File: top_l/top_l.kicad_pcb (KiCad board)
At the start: 2 copper layers, 128.4 x 119.3 mm, 31 parts, among them SW29 SW_Push, SW30 SW_Push, SW31 SW_Push, SW32 SW_Push, SW33 SW_Push, SW34 SW_Push, SW35 SW_Push, SW36 SW_Push, SW37 SW_Push, SW38 SW_Push, SW39 SW_Push, SW40 SW_Push, SW41 SW_Push, SW42 SW_Push, SW43 SW_Push, SW44 SW_Push, SW45 SW_Push, SW46 SW_Push, SW47 SW_Push, SW48 SW_Push, SW49 SW_Push, SW50 SW_Push, SW51 SW_Push, SW52 SW_Push, SW53 SW_Push, SW54 SW_Push, SW55 SW_Push

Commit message: feat: add switch plate
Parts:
- moved SW52 115.8 mm to (86.0, 66.9)
- moved SW53 115.8 mm to (86.0, 83.4)
- moved SW54 115.8 mm to (86.0, 99.9)
- moved SW55 115.8 mm to (86.0, 116.4)
- moved Ref** 99.2 mm to (94.3, 46.3)
- moved Ref** 90.9 mm to (189.3, 124.3)
- moved SW48 82.8 mm to (102.5, 66.9)
- moved SW49 82.8 mm to (102.5, 83.4)
- moved SW50 82.8 mm to (102.5, 99.9)
- moved SW51 82.8 mm to (102.5, 116.4)
- moved SW33 62.9 mm to (175.3, 136.8), turned to -15 degrees
- moved Ref** 58.9 mm to (173.3, 42.3)
- moved Ref** 54.2 mm to (116.8, 122.8)
- moved SW44 49.7 mm to (119.1, 50.5)
- moved SW45 49.7 mm to (119.1, 67.0)
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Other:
- outline, holes or cut-outs redrawn

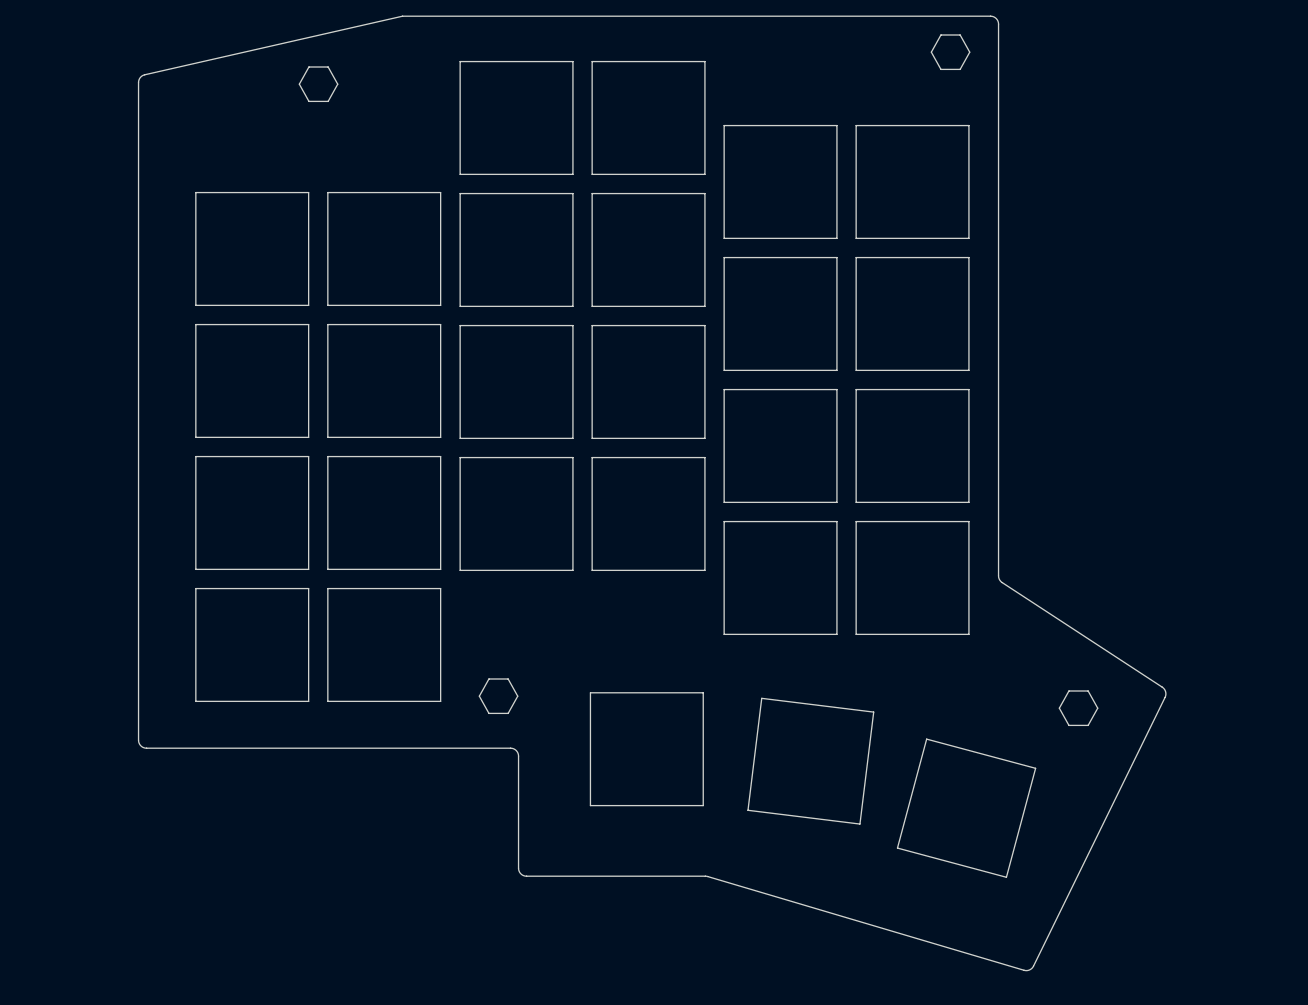
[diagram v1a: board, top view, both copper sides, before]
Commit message: feat: add hole to switch plate
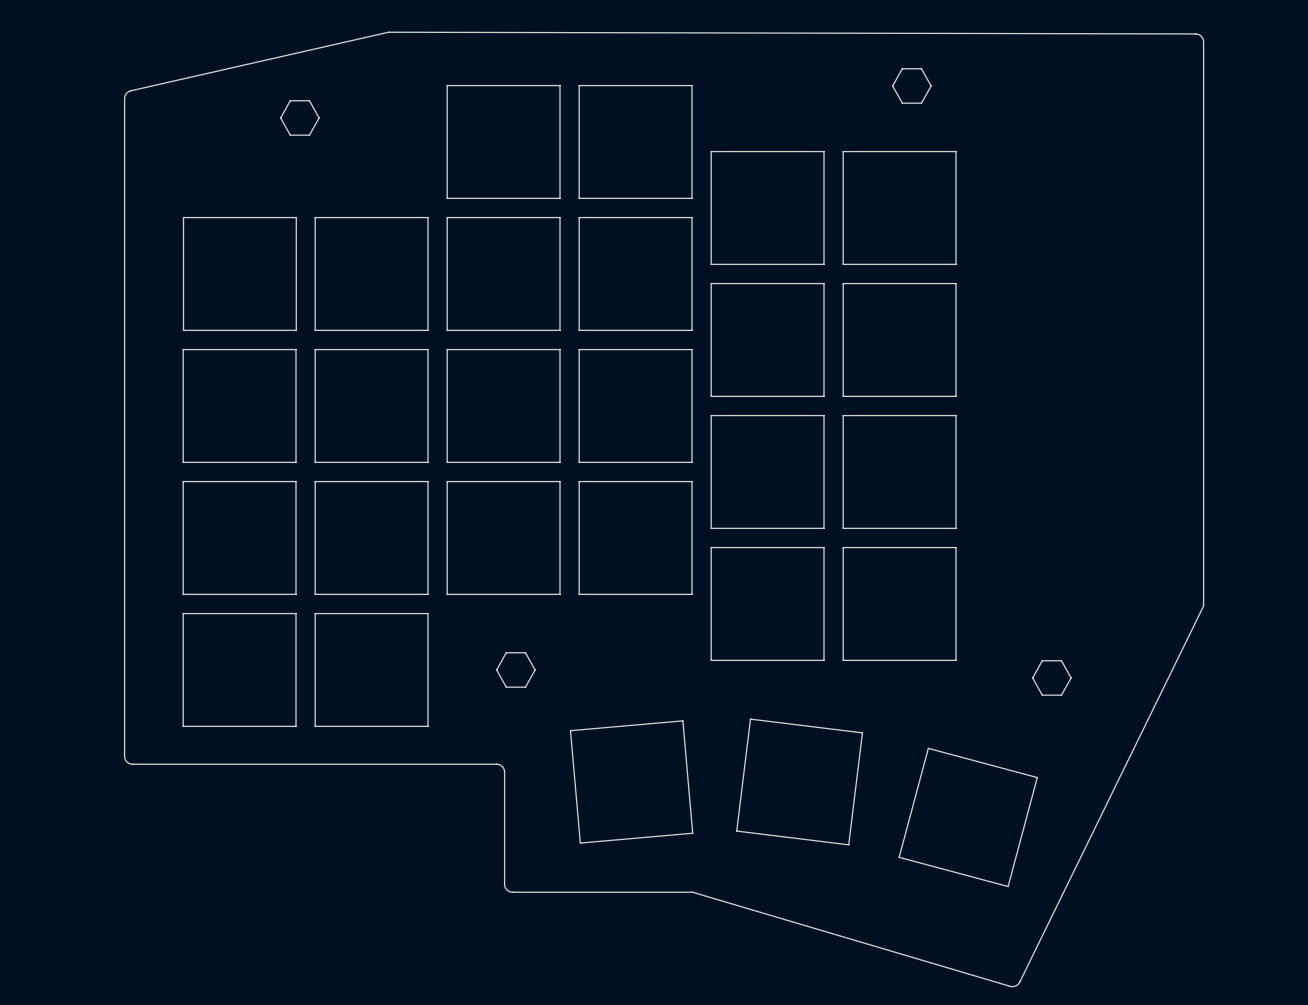
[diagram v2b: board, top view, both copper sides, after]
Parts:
- removed the Ref** at (173.3, 42.3)
- removed the Ref** at (189.3, 124.3)
- removed the Ref** at (94.3, 46.3)
- removed the Ref** at (116.8, 122.8)
- removed SW29, SW30, SW31, SW32, SW33, SW34, SW35, SW36, SW37, SW38, SW39, SW40, SW41, SW42, SW43, SW44, SW45, SW46, SW47, SW48, SW49, SW50, SW51, SW52, SW53, SW54, SW55: SW_Push, kbd_SW_Hole:SW_Hole_1u_16.5
- added Ref**: Val**, kbd_Hole:m2_Spacer_Hole_hex, F.Cu at (186.0, 120.5)
- added Ref**: Val**, kbd_Hole:m2_Spacer_Hole_hex, F.Cu at (92.0, 50.5)
- added Ref**: Val**, kbd_Hole:m2_Spacer_Hole_hex, F.Cu at (119.0, 119.5)
- added Ref**: Val**, kbd_Hole:m2_Spacer_Hole_hex, F.Cu at (168.5, 46.5)
- added SW1: SW_Push, kbd_SW_Hole:SW_Hole_1u_16.5, F.Cu at (84.5, 70.0)
- added SW10: SW_Push, kbd_SW_Hole:SW_Hole_1u_16.5, F.Cu at (134.0, 70.0)
- added SW11: SW_Push, kbd_SW_Hole:SW_Hole_1u_16.5, F.Cu at (150.5, 78.2)
- added SW12: SW_Push, kbd_SW_Hole:SW_Hole_1u_16.5, F.Cu at (167.0, 78.2)
- added SW13: SW_Push, kbd_SW_Hole:SW_Hole_1u_16.5, F.Cu at (84.5, 103.0)
- added SW14: SW_Push, kbd_SW_Hole:SW_Hole_1u_16.5, F.Cu at (101.0, 103.0)
- added SW15: SW_Push, kbd_SW_Hole:SW_Hole_1u_16.5, F.Cu at (117.5, 86.5)
- added SW16: SW_Push, kbd_SW_Hole:SW_Hole_1u_16.5, F.Cu at (134.0, 86.5)
- added SW17: SW_Push, kbd_SW_Hole:SW_Hole_1u_16.5, F.Cu at (150.5, 94.8)
- added SW18: SW_Push, kbd_SW_Hole:SW_Hole_1u_16.5, F.Cu at (167.0, 94.8)
- added SW19: SW_Push, kbd_SW_Hole:SW_Hole_1u_16.5, F.Cu at (84.5, 119.5)
- added SW2: SW_Push, kbd_SW_Hole:SW_Hole_1u_16.5, F.Cu at (101.0, 70.0)
- added SW20: SW_Push, kbd_SW_Hole:SW_Hole_1u_16.5, F.Cu at (101.0, 119.5)
- added SW21: SW_Push, kbd_SW_Hole:SW_Hole_1u_16.5, F.Cu at (117.5, 103.0)
- added SW22: SW_Push, kbd_SW_Hole:SW_Hole_1u_16.5, F.Cu at (134.0, 103.0)
- added SW23: SW_Push, kbd_SW_Hole:SW_Hole_1u_16.5, F.Cu at (150.5, 111.2)
- added SW24: SW_Push, kbd_SW_Hole:SW_Hole_1u_16.5, F.Cu at (167.0, 111.2)
- added SW25: SW_Push, kbd_SW_Hole:SW_Hole_1u_16.5, F.Cu at (133.5, 133.5)
- added SW26: SW_Push, kbd_SW_Hole:SW_Hole_1u_16.5, F.Cu at (154.5, 133.5)
- added SW27: SW_Push, kbd_SW_Hole:SW_Hole_1u_16.5, F.Cu at (175.5, 137.9)
- added SW3: SW_Push, kbd_SW_Hole:SW_Hole_1u_16.5, F.Cu at (117.5, 53.5)
- added SW4: SW_Push, kbd_SW_Hole:SW_Hole_1u_16.5, F.Cu at (134.0, 53.5)
- added SW5: SW_Push, kbd_SW_Hole:SW_Hole_1u_16.5, F.Cu at (150.5, 61.8)
- added SW6: SW_Push, kbd_SW_Hole:SW_Hole_1u_16.5, F.Cu at (167.0, 61.8)
- added SW7: SW_Push, kbd_SW_Hole:SW_Hole_1u_16.5, F.Cu at (84.5, 86.5)
- added SW8: SW_Push, kbd_SW_Hole:SW_Hole_1u_16.5, F.Cu at (101.0, 86.5)
- added SW9: SW_Push, kbd_SW_Hole:SW_Hole_1u_16.5, F.Cu at (117.5, 70.0)
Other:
- board size 128.4 x 119.3 mm -> 134.9 x 119.3 mm

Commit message: refactor: top left plate
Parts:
- removed Ref** (x4): Val**, kbd_Hole:m2_Spacer_Hole_hex
- removed SW22, SW23, SW24, SW25, SW26, SW27: SW_Push, kbd_SW_Hole:SW_Hole_1u_16.5
- moved SW19 75.1 mm to (152.5, 87.9)
- moved SW3 71.0 mm to (70.0, 106.4), turned to 180 degrees
- moved SW5 69.8 mm to (86.5, 89.9)
- moved SW6 64.0 mm to (103.0, 65.4)
- moved SW21 54.3 mm to (165.3, 128.6), turned to -15 degrees
- moved SW20 53.7 mm to (152.5, 104.4)
- moved SW12 51.5 mm to (119.5, 98.4)
- moved SW4 51.4 mm to (86.5, 73.4)
- moved SW13 50.1 mm to (130.6, 122.3), turned to 177.5 degrees
- moved SW14 48.6 mm to (136.0, 69.4)
- moved SW9 47.7 mm to (86.5, 106.4)
- moved SW2 36.8 mm to (70.0, 89.9), turned to 180 degrees
- moved SW11 31.1 mm to (119.5, 81.9)
- moved SW17 29.9 mm to (148.2, 124.5), turned to -10 degrees
- moved SW18 27.5 mm to (152.5, 71.4)
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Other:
- board size 134.9 x 119.3 mm -> 126.3 x 102.6 mm

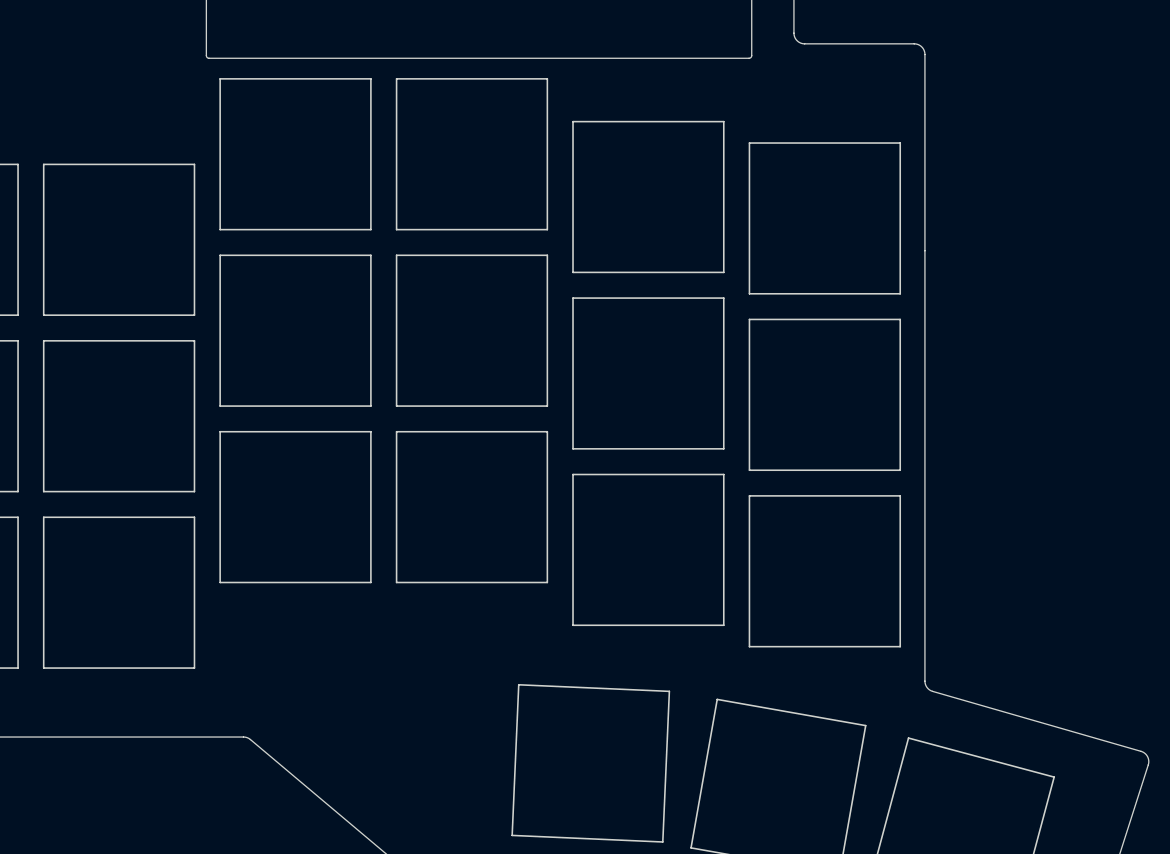
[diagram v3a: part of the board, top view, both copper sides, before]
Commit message: feat: add screw
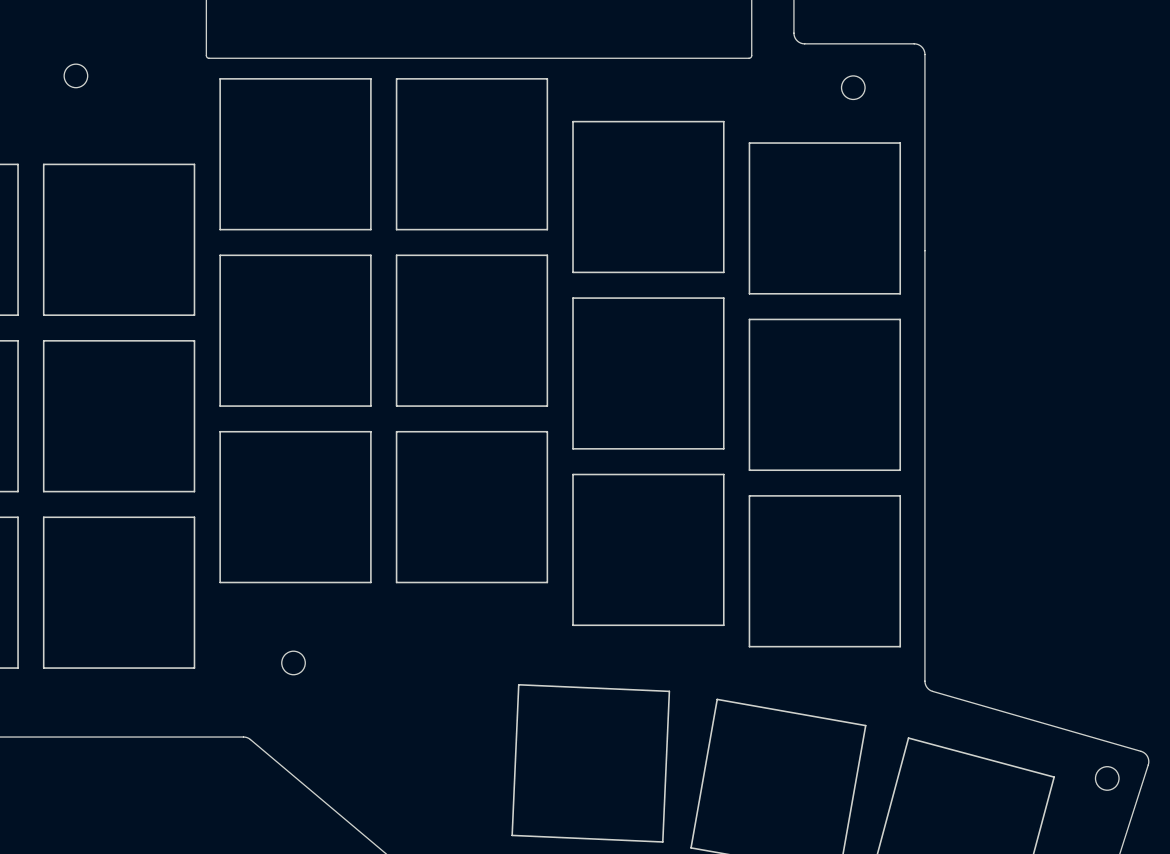
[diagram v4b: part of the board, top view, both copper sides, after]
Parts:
- added Ref**: Val**, kbd_Hole:m2_Screw_Hole, F.Cu at (178.9, 123.8)
- added Ref**: Val**, kbd_Hole:m2_Screw_Hole, F.Cu at (102.8, 113.0)
- added Ref**: Val**, kbd_Hole:m2_Screw_Hole, F.Cu at (82.5, 58.0)
- added Ref**: Val**, kbd_Hole:m2_Screw_Hole, F.Cu at (155.2, 59.1)

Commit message: fix: remake top plate
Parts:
- moved SW6 44.2 mm to (86.5, 106.4)
- moved SW9 18.2 mm to (103.0, 98.5), turned to 180 degrees
- moved SW7 16.4 mm to (103.0, 65.5), turned to 180 degrees
- moved SW8 16.4 mm to (103.0, 82.0), turned to 180 degrees
- moved Ref** 2.73 mm to (85.0, 59.1)
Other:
- board size 126.3 x 102.6 mm -> 128.5 x 102.6 mm
